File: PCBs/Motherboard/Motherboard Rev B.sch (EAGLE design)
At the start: 60 parts, among them J1 MOLEX_504050-0591, J2 MOLEX_504050-0491, Q1 16M, Q2 32.768k, U1 Value, X1 2514-5

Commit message: Add I2C pullups
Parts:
- added R21, R22, R23, R24: 10k, resistor:R-US_R0805
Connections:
- net 3V3_UC: now also R21.2, R22.1, R23.2, R24.1
- net SCL_ANT: now also R24.2
- net SCL_EPS: now also R22.2
- net SDA_ANT: now also R23.1
- net SDA_EPS: now also R21.1
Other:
- moved on the sheet: J2, JTAG_PWR, R13, R14, X1

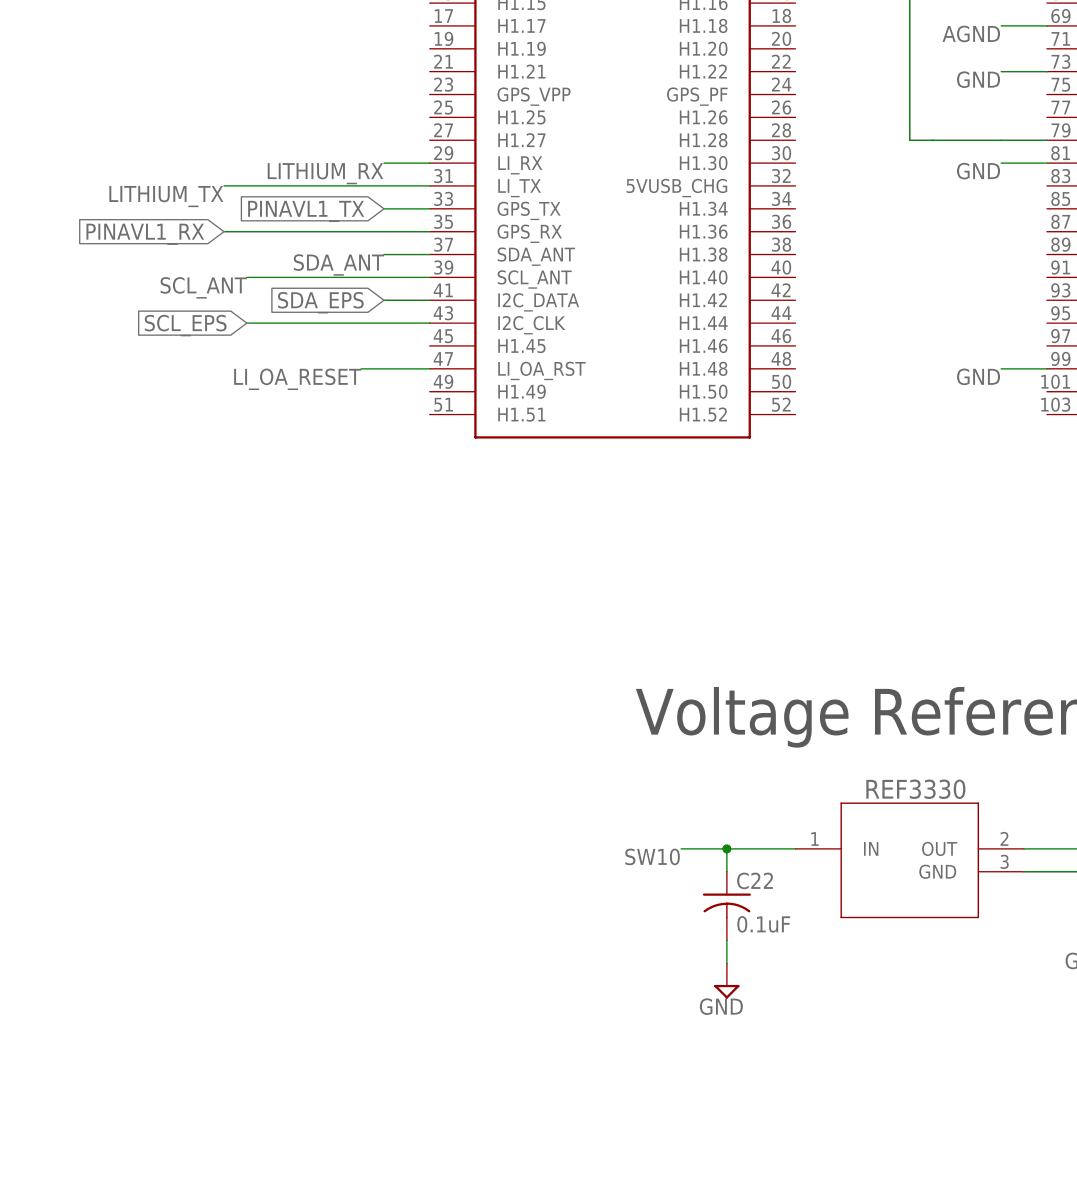
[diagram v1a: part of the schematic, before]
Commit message: Add external 5V charging jack
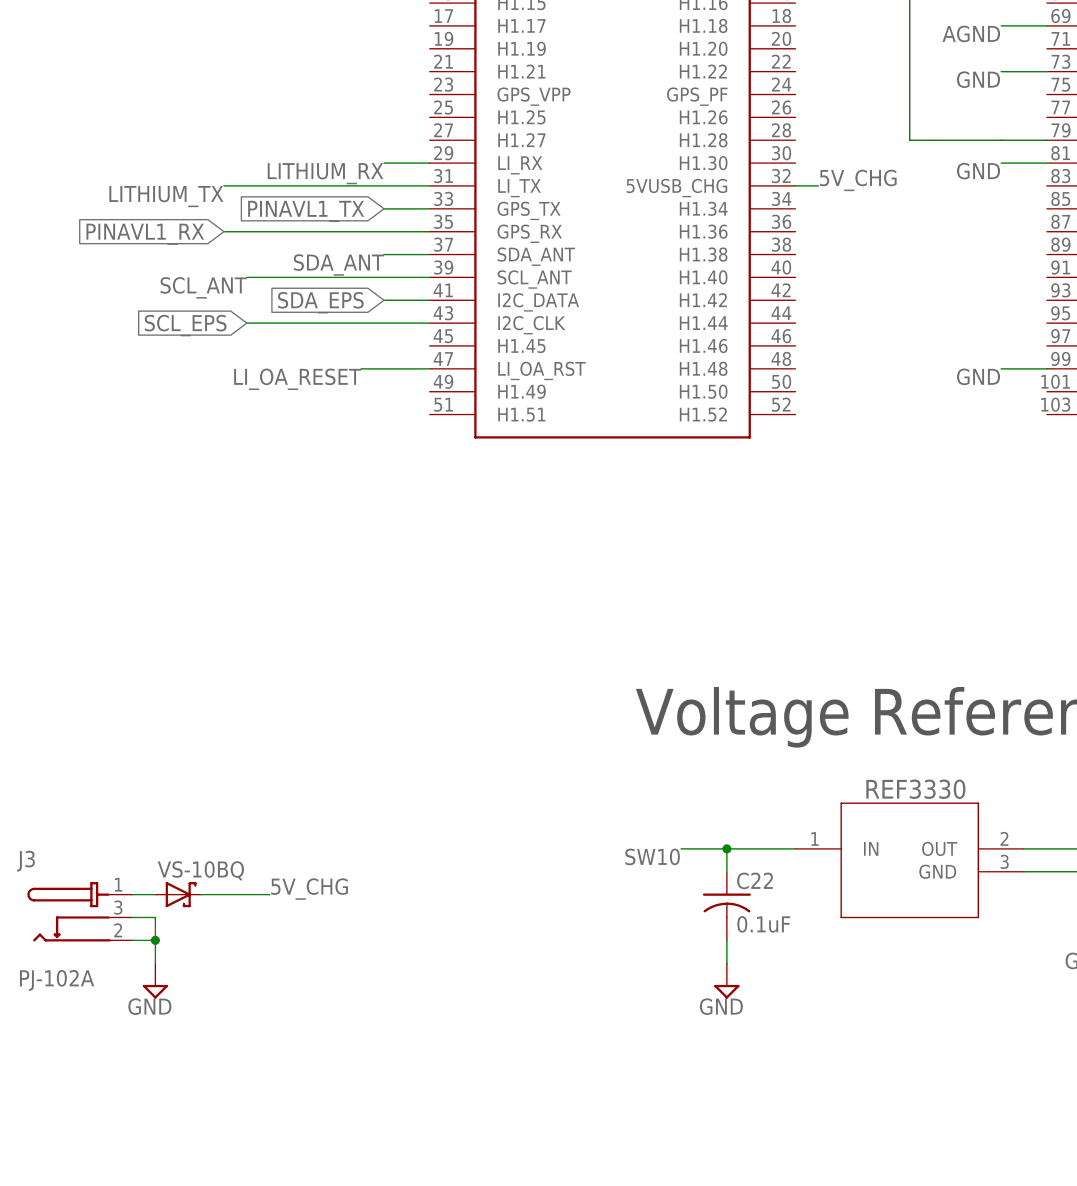
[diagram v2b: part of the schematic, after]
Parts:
- added J3: PJ-102A, PJ-102A:PJ-102A
- added VS-10BQ: 10BQ015HM3, Vishay 10BQ015HM3:10BQ015HM3
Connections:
- new net 5V_CHG: U$1.5VUSB_CHG, VS-10BQ.C
- new net N$14: J3.1, VS-10BQ.A
- net GND: now also J3.2, J3.3
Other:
- note added: "DC Power"
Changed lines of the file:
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@@
 <part name="R23" library="resistor" library_urn="urn:adsk.eagle:library:348" deviceset="R-US_" device="R0805" package3d_urn="urn:adsk.eagle:package:23553/2" value="10k"/>
 <part name="R24" library="resistor" library_urn="urn:adsk.eagle:library:348" deviceset="R-US_" device="R0805" package3d_urn="urn:adsk.eagle:package:23553/2" value="10k"/>
+<part name="J3" library="PJ-102A" deviceset="PJ-102A" device=""/>
+<part name="SUPPLY14" library="supply2" library_urn="urn:adsk.eagle:library:372" deviceset="GND" device=""/>
+<part name="VS-10BQ" library="Vishay 10BQ015HM3" deviceset="10BQ015HM3" device=""/>
 </parts>
 <sheets>
@@
 <text x="231.14" y="-78.74" size="1.778" layer="97">Av=10</text>
 <text x="274.32" y="91.44" size="5.08" layer="97">Antenna</text>
+<text x="50.8" y="22.86" size="5.08" layer="120">DC Power</text>
 </plain>
 <instances>
@@
 <instance part="R23" gate="G$1" x="756.92" y="93.98" rot="R90"/>
 <instance part="R24" gate="G$1" x="756.92" y="76.2" rot="R90"/>
+<instance part="J3" gate="G$1" x="63.5" y="12.7"/>
+<instance part="SUPPLY14" gate="GND" x="71.12" y="2.54" rot="MR0"/>
+<instance part="VS-10BQ" gate="G$1" x="73.66" y="12.7"/>
 </instances>
 <busses>
@@
 <wire x1="279.4" y1="76.2" x2="271.78" y2="76.2" width="0.1524" layer="91"/>
 <wire x1="271.78" y1="76.2" x2="271.78" y2="71.12" width="0.1524" layer="91"/>
+</segment>
+<segment>
+<pinref part="J3" gate="G$1" pin="2"/>
+<wire x1="68.58" y1="7.62" x2="71.12" y2="7.62" width="0.1524" layer="91"/>
+<pinref part="J3" gate="G$1" pin="3"/>
+<wire x1="68.58" y1="10.16" x2="71.12" y2="10.16" width="0.1524" layer="91"/>
+<wire x1="71.12" y1="10.16" x2="71.12" y2="7.62" width="0.1524" layer="91"/>
+<wire x1="71.12" y1="7.62" x2="71.12" y2="5.08" width="0.1524" layer="91"/>
+<junction x="71.12" y="7.62"/>
+<pinref part="SUPPLY14" gate="GND" pin="GND"/>
 </segment>
 </net>
@@
 </segment>
 </net>
+<net name="5V_CHG" class="0">
+<segment>
+<pinref part="U$1" gate="A" pin="5VUSB_CHG"/>
+<wire x1="142.24" y1="91.44" x2="144.78" y2="91.44" width="0.1524" layer="91"/>
+<label x="144.78" y="91.44" size="1.778" layer="95"/>
+</segment>
+<segment>
+<pinref part="VS-10BQ" gate="G$1" pin="C"/>
+<wire x1="76.2" y1="12.7" x2="83.82" y2="12.7" width="0.1524" layer="91"/>
+<label x="83.82" y="12.7" size="1.778" layer="95"/>
+</segment>
+</net>
+<net name="N$14" class="0">
+<segment>
+<pinref part="J3" gate="G$1" pin="1"/>
+<pinref part="VS-10BQ" gate="G$1" pin="A"/>
+<wire x1="68.58" y1="12.7" x2="71.12" y2="12.7" width="0.1524" layer="91"/>
+</segment>
+</net>

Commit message: Swap JTAG UART and piNAV comm channels
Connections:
- net JTAG_RXD: now also U1.P2.0_TB0.6_UCA0TXD_UCA0SIMO_TB0CLK_ACLK; no longer U1.P2.5_TB0.0_UCA1TXD_UCA1SIMO
- net JTAG_TXD: now also U1.P2.1_TB0.0_UCA0RXD_UCA0SOMI; no longer U1.P2.6_TB0.1_UCA1RXD_UCA1SOMI
- net PINAVL1_RX: now also U1.P2.5_TB0.0_UCA1TXD_UCA1SIMO; no longer U1.P2.0_TB0.6_UCA0TXD_UCA0SIMO_TB0CLK_ACLK
- net PINAVL1_TX: now also U1.P2.6_TB0.1_UCA1RXD_UCA1SOMI; no longer U1.P2.1_TB0.0_UCA0RXD_UCA0SOMI
- net SCL_ANT: no longer U$1.SCL_ANT
- net SDA_ANT: no longer U$1.SDA_ANT
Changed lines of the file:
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@@
 </segment>
 <segment>
-<pinref part="U1" gate="A" pin="P2.0_TB0.6_UCA0TXD_UCA0SIMO_TB0CLK_ACLK"/>
-<wire x1="698.5" y1="142.24" x2="734.06" y2="142.24" width="0.1524" layer="91"/>
-<label x="734.06" y="142.24" size="1.778" layer="95"/>
+<pinref part="U1" gate="A" pin="P2.5_TB0.0_UCA1TXD_UCA1SIMO"/>
+<wire x1="698.5" y1="129.54" x2="711.2" y2="129.54" width="0.1524" layer="91"/>
+<label x="711.2" y="129.54" size="1.778" layer="95"/>
 </segment>
 </net>
@@
 </segment>
 <segment>
-<pinref part="U1" gate="A" pin="P2.1_TB0.0_UCA0RXD_UCA0SOMI"/>
-<wire x1="698.5" y1="139.7" x2="734.06" y2="139.7" width="0.1524" layer="91"/>
-<label x="734.06" y="139.7" size="1.778" layer="95"/>
+<pinref part="U1" gate="A" pin="P2.6_TB0.1_UCA1RXD_UCA1SOMI"/>
+<wire x1="698.5" y1="127" x2="711.2" y2="127" width="0.1524" layer="91"/>
+<label x="711.2" y="127" size="1.778" layer="95"/>
 </segment>
 </net>
@@
 <net name="JTAG_RXD" class="0">
 <segment>
-<pinref part="U1" gate="A" pin="P2.5_TB0.0_UCA1TXD_UCA1SIMO"/>
-<wire x1="698.5" y1="129.54" x2="711.2" y2="129.54" width="0.1524" layer="91"/>
-<label x="711.2" y="129.54" size="1.778" layer="95"/>
-</segment>
-<segment>
 <pinref part="R13" gate="G$1" pin="1"/>
 <wire x1="383.54" y1="12.7" x2="383.54" y2="10.16" width="0.1524" layer="91"/>
 <wire x1="383.54" y1="10.16" x2="391.16" y2="10.16" width="0.1524" layer="91"/>
 <label x="391.16" y="10.16" size="1.778" layer="95"/>
+</segment>
+<segment>
+<pinref part="U1" gate="A" pin="P2.0_TB0.6_UCA0TXD_UCA0SIMO_TB0CLK_ACLK"/>
+<wire x1="698.5" y1="142.24" x2="711.2" y2="142.24" width="0.1524" layer="91"/>
+<label x="711.2" y="142.24" size="1.778" layer="95"/>
 </segment>
 </net>
@@
 <net name="JTAG_TXD" class="0">
 <segment>
-<pinref part="U1" gate="A" pin="P2.6_TB0.1_UCA1RXD_UCA1SOMI"/>
-<wire x1="698.5" y1="127" x2="711.2" y2="127" width="0.1524" layer="91"/>
-<label x="711.2" y="127" size="1.778" layer="95"/>
-</segment>
-<segment>
 <pinref part="R14" gate="G$1" pin="1"/>
 <wire x1="375.92" y1="12.7" x2="375.92" y2="7.62" width="0.1524" layer="91"/>
 <wire x1="375.92" y1="7.62" x2="391.16" y2="7.62" width="0.1524" layer="91"/>
 <label x="391.16" y="7.62" size="1.778" layer="95"/>
+</segment>
+<segment>
+<pinref part="U1" gate="A" pin="P2.1_TB0.0_UCA0RXD_UCA0SOMI"/>
+<wire x1="698.5" y1="139.7" x2="711.2" y2="139.7" width="0.1524" layer="91"/>
+<label x="711.2" y="139.7" size="1.778" layer="95"/>
 </segment>
 </net>
@@
 </segment>
 <segment>
-<pinref part="U$1" gate="A" pin="SDA_ANT"/>
-<wire x1="101.6" y1="83.82" x2="96.52" y2="83.82" width="0.1524" layer="91"/>
-<label x="96.52" y="83.82" size="1.778" layer="95" rot="R180"/>
-</segment>
-<segment>
 <pinref part="J2" gate="G$1" pin="3"/>
 <wire x1="292.1" y1="78.74" x2="276.86" y2="78.74" width="0.1524" layer="91"/>
@@
 </segment>
 <segment>
-<pinref part="U$1" gate="A" pin="SCL_ANT"/>
-<wire x1="101.6" y1="81.28" x2="81.28" y2="81.28" width="0.1524" layer="91"/>
-<label x="81.28" y="81.28" size="1.778" layer="95" rot="R180"/>
-</segment>
-<segment>

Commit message: Add external UART connector
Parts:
- added EXT_UART: 90121-0763, Molex 90121-0763:90121-0763
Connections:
- net EXT_RXD: now also EXT_UART.3
- net EXT_TXD: now also EXT_UART.2
- net GND: now also EXT_UART.1
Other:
- note added: "External UART"
- note removed: "Add external UART pins"
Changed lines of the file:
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@@
 <part name="SUPPLY14" library="supply2" library_urn="urn:adsk.eagle:library:372" deviceset="GND" device=""/>
 <part name="VS-10BQ" library="Vishay 10BQ015HM3" deviceset="10BQ015HM3" device=""/>
+<part name="EXT_UART" library="Molex 90121-0763" deviceset="90121-0763" device=""/>
+<part name="SUPPLY33" library="supply2" library_urn="urn:adsk.eagle:library:372" deviceset="GND" device=""/>
+<part name="SUPPLY34" library="supply2" library_urn="urn:adsk.eagle:library:372" deviceset="GND" device=""/>
 </parts>
 <sheets>
@@
 <text x="360.68" y="-30.48" size="5.08" layer="97">Temperature</text>
 <text x="124.46" y="30.48" size="5.08" layer="97">Voltage Reference</text>
-<text x="716.28" y="99.06" size="1.778" layer="91">Add external UART pins</text>
 <text x="231.14" y="-78.74" size="1.778" layer="97">Av=10</text>
 <text x="274.32" y="91.44" size="5.08" layer="97">Antenna</text>
 <text x="50.8" y="22.86" size="5.08" layer="120">DC Power</text>
+<text x="347.98" y="99.06" size="5.08" layer="97">External UART</text>
 </plain>
 <instances>
@@
 <instance part="SUPPLY14" gate="GND" x="71.12" y="2.54" rot="MR0"/>
 <instance part="VS-10BQ" gate="G$1" x="73.66" y="12.7"/>
+<instance part="EXT_UART" gate="G$1" x="350.52" y="76.2"/>
+<instance part="SUPPLY33" gate="GND" x="365.76" y="73.66"/>
+<instance part="SUPPLY34" gate="GND" x="279.4" y="68.58"/>
 </instances>
 <busses>
@@
 </segment>
 <segment>
-<wire x1="271.78" y1="71.12" x2="271.78" y2="68.58" width="0.1524" layer="91"/>
-<label x="271.78" y="68.58" size="1.778" layer="95" rot="R180"/>
 <pinref part="J2" gate="G$1" pin="4"/>
 <wire x1="292.1" y1="76.2" x2="279.4" y2="76.2" width="0.1524" layer="91"/>
-<wire x1="279.4" y1="76.2" x2="271.78" y2="76.2" width="0.1524" layer="91"/>
-<wire x1="271.78" y1="76.2" x2="271.78" y2="71.12" width="0.1524" layer="91"/>
+<pinref part="SUPPLY34" gate="GND" pin="GND"/>
+<wire x1="279.4" y1="76.2" x2="279.4" y2="71.12" width="0.1524" layer="91"/>
 </segment>
 <segment>
@@
 <junction x="71.12" y="7.62"/>
 <pinref part="SUPPLY14" gate="GND" pin="GND"/>
+</segment>
+<segment>
+<pinref part="EXT_UART" gate="G$1" pin="1"/>
+<wire x1="360.68" y1="78.74" x2="365.76" y2="78.74" width="0.1524" layer="91"/>
+<wire x1="365.76" y1="78.74" x2="365.76" y2="76.2" width="0.1524" layer="91"/>
+<pinref part="SUPPLY33" gate="GND" pin="GND"/>
 </segment>
 </net>
@@
 <label x="711.2" y="96.52" size="1.778" layer="95"/>
 </segment>
+<segment>
+<pinref part="EXT_UART" gate="G$1" pin="3"/>
+<wire x1="360.68" y1="88.9" x2="365.76" y2="88.9" width="0.1524" layer="91"/>
+<label x="365.76" y="88.9" size="1.778" layer="95"/>
+</segment>
 </net>
 <net name="EXT_TXD" class="0">
@@
 <label x="711.2" y="93.98" size="1.778" layer="95"/>
 </segment>
-</net>
+<segment>
+<pinref part="EXT_UART" gate="G$1" pin="2"/>
+<wire x1="360.68" y1="83.82" x2="365.76" y2="83.82" width="0.1524" layer="91"/>
+<label x="365.76" y="83.82" size="1.778" layer="95"/>
+</segment>
+</net>

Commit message: Add RBF mount, replace strain gauge with temp sensor, clean up crossed traces, dimension PCB to accomodate wiring
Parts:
- removed AD8228: AD8228BRZ, AD8228:AD8228BRZ
- removed C21: 0.1uF, resistor:C-USC0805
- removed R11, R17, R18: 10k, resistor:R-US_R0805
- removed R12: 100, resistor:R-US_R0805
- removed R15, R16, R19, R20: 0, resistor:R-US_R0805
- J1: value MOLEX_504050-0591 -> MOLEX_504050-0691; device Molex 504050:MOLEX_504050-0591 -> Molex 504050:MOLEX_504050-0691
- R10: value 10k -> 100
- R9: value 350 -> 100
- renumbered J3 to 5V_DC
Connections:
- removed net 1V5: AD8228.REF, TLV2452.IN-1, TLV2452.OUT1
- removed net 1V5_REF: R17.1, R18.2, TLV2452.IN+1
- removed net N$10: AD8228.IN-, AD8228.VOUT, R10.2, R11.1, R15.1
- removed net N$15: R19.1, TLV2452.IN-2, TLV2452.OUT2
- removed net N$17: R20.1, TLV2452.IN+2
- removed net N$6: AD8228.IN+, R16.1
- removed net STRAIN_OUT: R15.2, U1.P3.1_A13_C13
- removed net STRN: J1.5, R16.2, R9.2
- removed net TEMP: J1.2, R12.2, R20.2
- removed net TEMP_OUT: R19.2, U1.P3.2_A14_C14
- removed net TEMP_RET: J1.3
- new net TMP1: J1.2, TLV2452.IN+1
- new net TMP1_OUT: TLV2452.IN-1, TLV2452.OUT1, U1.P3.1_A13_C13
- new net TMP1_RET: J1.3, R9.2
- new net TMP2: J1.5, TLV2452.IN+2
- new net TMP2_OUT: TLV2452.IN-2, TLV2452.OUT2, U1.P3.2_A14_C14
- new net TMP2_RET: J1.6, R10.2
- net 3V: no longer R11.2, R17.2
- net GND: no longer AD8228.VS-, C21.2, R12.1, R18.1
- net SW10: no longer AD8228.VS+, C21.1
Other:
- note removed: "Av=10"
- note removed: "Strain Gauge"
- moved on the sheet: C24, R10, R9, TLV2452

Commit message: Rework layout for tighter traces
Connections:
- net AGND: no longer U$1.GND1, U$1.GND2, U$1.GND3, U$1.GND5
- net EXT_RXD: now also EXT_UART.2; no longer EXT_UART.3
- net EXT_TXD: now also EXT_UART.3; no longer EXT_UART.2
- net GND: now also U$1.GND1, U$1.GND2, U$1.GND3, U$1.GND5
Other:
- note removed: "Not sure if we need FSYNC, INT"
- moved on the sheet: 5V_DC, C1, C10, C11, C13, C14, C16, C2, C20, C22, C24, C3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

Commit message: Completed first draft
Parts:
- renumbered U1 to MSP430, X1 to JTAG
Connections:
- net N$12 renamed HFXIN
- net N$13 renamed LFXOUT
- net N$4 renamed HFXOUT
- net N$9 renamed LFXIN
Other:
- moved on the sheet: Q1

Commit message: Add test pads, RBF->DF13 wiring, update power distribution, breakout extra I/O pins
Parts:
- added 3V, 3V3, 3V3_ALT, 3V3_SD, 3V3_UC, 3VREF, 5V_CHG, 7.4, 7.5, 7.6, 7.7, ANT_SCL, ANT_SDA, EPS_SCL, EPS_SDA, GPS_RX, GPS_TX, JTAG_RX, JTAG_TX, LI_RX, LI_TX, OA_RST, SD_DET, SW10, SW5, SW6, SW8, TCK, TDIO, TMP1, TMP2: TPSQTP10SQ, testpad:TPSQTP10SQ
- added C21, C25, C26: 0.1uF, resistor:C-USC0805
- added IMU_CLK, IMU_MISO, IMU_MOSI: TPSQTP06SQ, testpad:TPSQTP06SQ
- added RBF: DF13-3P-1.25V, con-hirose-df13:DF13-3P-1.25V
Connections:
- new net 3V3BUS2: 3V3_ALT.TP, U$1.3V3BUS2
- new net N$10: 7.6.TP, MSP430.P7.6_A18
- new net N$12: 7.7.TP, MSP430.P7.7_A19
- new net N$4: SW6.TP, U$1.SW6_5V
- new net N$6: 7.4.TP, MSP430.P7.4__TA4.0_A16
- new net N$9: 7.5.TP, MSP430.P7.5_A17
- new net RBF_C: RBF.1
- new net RBF_NO: RBF.2
- new net SW8: SW8.TP, U$1.SW8_3V3
- net 3V: now also 3V.TP
- net 3V3: now also 3V3.TP
- net 3V3_SD: now also 3V3_SD.TP
- net 3V3_UC: now also 3V3_UC.TP
- net 3V_REF: now also 3VREF.TP
- net 5V_CHG: now also 5V_CHG.TP, C21.1
- net CLK_IMU: now also IMU_CLK.TP
- net GND: now also C21.2, C25.2, C26.2
- net JTAG_RXD: now also JTAG_RX.TP
- net JTAG_TXD: now also JTAG_TX.TP
- net LITHIUM_RX: now also LI_RX.TP
- net LITHIUM_TX: now also LI_TX.TP
- net LI_OA_RESET: now also OA_RST.TP
- net MISO_IMU: now also IMU_MISO.TP
- net MOSI_IMU: now also IMU_MOSI.TP
- net PINAVL1_RX: now also GPS_RX.TP
- net PINAVL1_TX: now also GPS_TX.TP
- net SBWTCK: now also TCK.TP
- net SBWTDIO: now also TDIO.TP
- net SCL_ANT: now also ANT_SCL.TP
- net SCL_EPS: now also EPS_SCL.TP
- net SDA_ANT: now also ANT_SDA.TP
- net SDA_EPS: now also EPS_SDA.TP
- net SD_DETECT: now also SD_DET.TP
- net SW10: now also SW10.TP
- net SW5: now also SW5.TP
- net TMP1: now also C25.1
- net TMP1_OUT: now also TMP1.TP
- net TMP2: now also C26.1
- net TMP2_OUT: now also TMP2.TP
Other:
- note added: "RBF"
- moved on the sheet: C1, C10, C11, C5, C6, C7, C8, C9, J2
